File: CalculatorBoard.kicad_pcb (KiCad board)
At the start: 2 copper layers, 81.3 x 83.8 mm, 62 parts, among them J1 Conn_01x07_Male, Q1 Q_NPN_EBC, Q10 Q_NPN_EBC, Q11 Q_NPN_EBC, Q12 Q_NPN_EBC, Q13 Q_NPN_EBC, Q14 Q_NPN_EBC, Q15 Q_NPN_EBC, Q16 Q_NPN_EBC, Q17 Q_NPN_EBC, Q18 Q_NPN_EBC, Q19 Q_NPN_EBC, Q2 Q_NPN_EBC, Q20 Q_NPN_EBC, Q21 Q_NPN_EBC, Q22 Q_NPN_EBC, Q3 Q_NPN_EBC, Q4 Q_NPN_EBC, Q5 Q_NPN_EBC, Q6 Q_NPN_EBC, Q7 Q_NPN_EBC, Q8 Q_NPN_EBC, Q9 Q_NPN_EBC

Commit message: fix pin 5 goof. Reroute some components.
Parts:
- moved R10 17.1 mm to (62.1, 86.4), turned to 270 degrees
- moved R16 16.8 mm to (43.2, 91.4), turned to 90 degrees
- moved Q13 15.9 mm to (51.1, 85.7)
- moved R25 15.1 mm to (28.1, 73.0), turned to 90 degrees
- moved R22 13.4 mm to (54.9, 79.4), turned to 0 degrees
- moved R19 12.7 mm to (54.6, 91.2)
- moved H2 12.2 mm to (21.1, 91.4)
- moved H1 12.1 mm to (95.5, 91.3)
- moved Q5 10.7 mm to (71.1, 65.6)
- moved R13 9.66 mm to (73.2, 75.8)
- moved R14 8.41 mm to (70.0, 86.4), turned to 270 degrees
- moved R24 7.38 mm to (34.7, 86.2)
- moved R30 5.89 mm to (28.5, 91.1)
- moved R35 5.21 mm to (21.6, 34.0), turned to 270 degrees
- moved Q9 4.32 mm to (64.0, 71.1)
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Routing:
- net Net-(Q4-Pad1): track 39.7 -> 21.6 mm
- net Net-(Q10-Pad1): track 85.9 -> 69.2 mm
- net Net-(Q5-Pad1): track 10.8 -> 23.0 mm
- net Net-(Q13-Pad3): track 20.8 -> 29.4 mm
- net Net-(Q5-Pad2): track 38.7 -> 31.5 mm
- net Net-(Q16-Pad1): track 17.8 -> 22.7 mm
- net Net-(Q15-Pad2): track 12.7 -> 8.15 mm
- net Net-(J1-Pad5): track 88.2 -> 92.5 mm
- net Net-(Q16-Pad2): track 12.7 -> 9.25 mm
- net Net-(Q9-Pad2): track 8.15 -> 11.5 mm
- net Net-(Q6-Pad1): track 21.2 -> 18.4 mm
- net Net-(Q10-Pad2): track 8.93 -> 6.14 mm
- net Net-(Q13-Pad2): track 9.61 -> 7.08 mm
- net Net-(Q2-Pad3): track 34.7 -> 32.5 mm
- net Net-(Q4-Pad2): track 9.78 -> 8.38 mm
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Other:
- board size 81.3 x 83.8 mm -> 81.3 x 73.7 mm

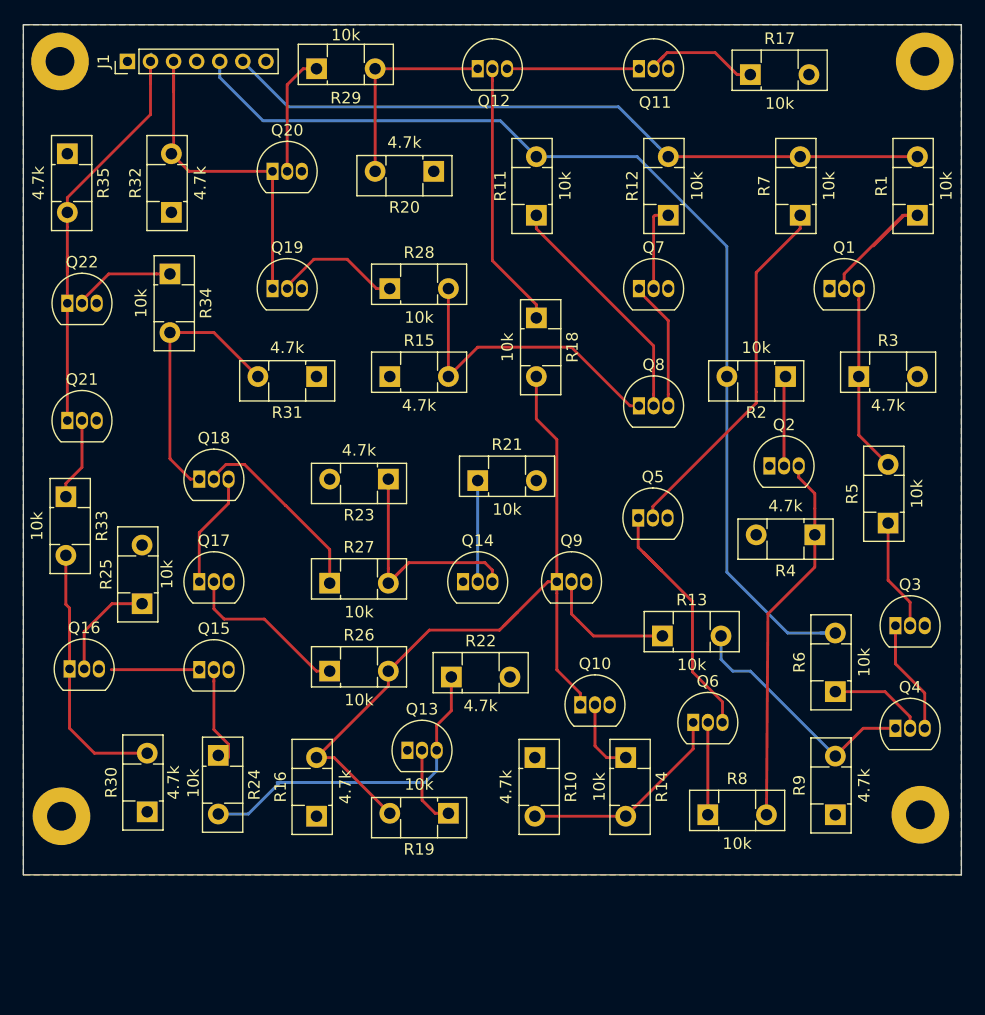
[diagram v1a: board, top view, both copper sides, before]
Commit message: change resistor size and shrink layout
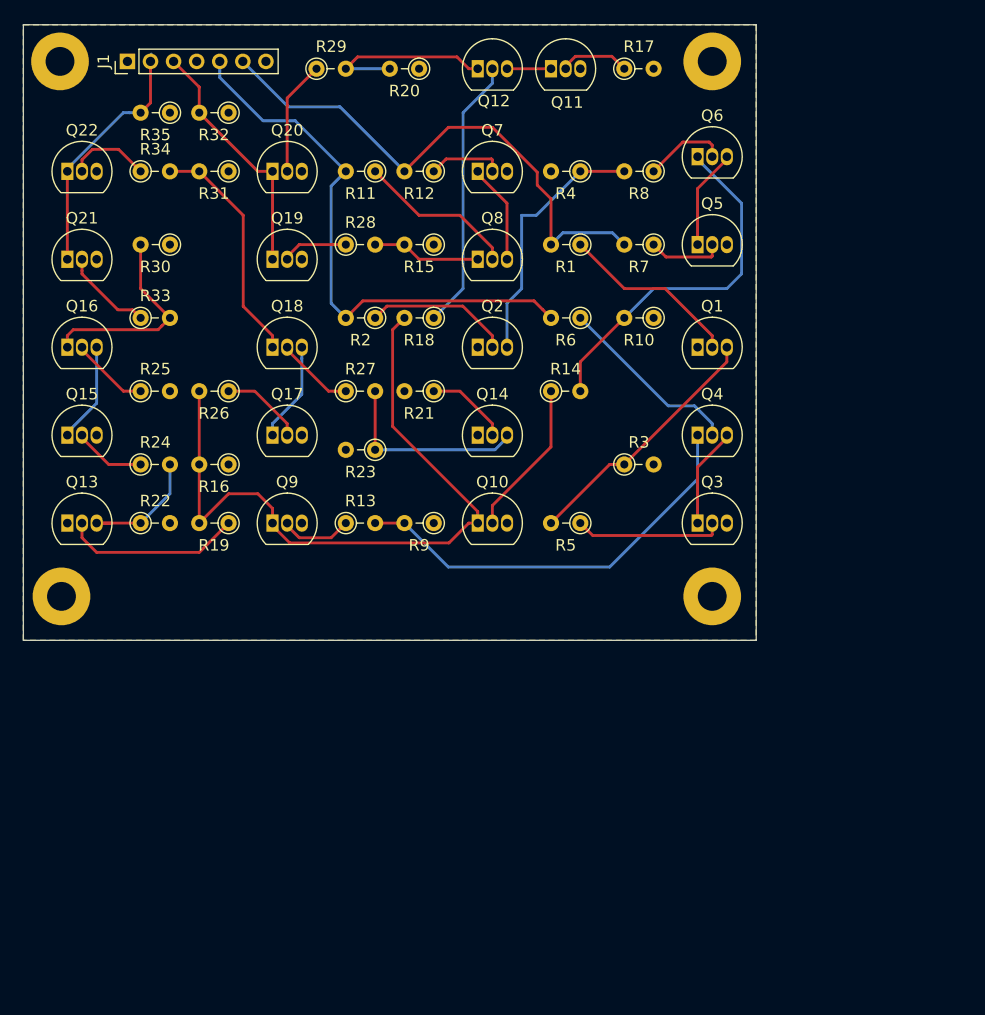
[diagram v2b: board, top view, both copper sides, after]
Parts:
- R1, R10, R11, R12, R13, R14, R15, R16, R17, R18, R19, R2, R20, R21, R22, R23, R24, R25, R26, R27, R28, R29, R3, R30, R31, R32, R33, R34, R35, R4, R5, R6, R7, R8, R9: footprint Package_TO_SOT_THT:TO-126-2_Vertical -> Resistor_THT:R_Axial_DIN0204_L3.6mm_D1.6mm_P2.54mm_Vertical
- moved R8 56.0 mm to (72.4, 35.6), turned to 180 degrees
- moved R30 49.2 mm to (30.5, 41.9), turned to 180 degrees
- moved Q6 49.0 mm to (76.2, 34.3)
- moved R9 43.0 mm to (53.3, 66.0), turned to 180 degrees
- moved R10 39.5 mm to (72.4, 48.3), turned to 180 degrees
- moved R6 39.2 mm to (66.0, 48.3), turned to 180 degrees
- moved R4 37.5 mm to (66.0, 35.6)
- moved R2 35.9 mm to (48.3, 48.3)
- moved Q13 35.4 mm to (21.6, 66.0)
- moved R14 32.4 mm to (63.5, 54.6), turned to 0 degrees
- moved R19 31.5 mm to (35.6, 66.0)
- moved R16 31.4 mm to (35.6, 61.0), turned to 180 degrees
- moved Q4 30.6 mm to (76.2, 58.4)
- moved R22 30.0 mm to (27.9, 66.0)
- moved R1 29.3 mm to (66.0, 41.9), turned to 180 degrees
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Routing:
- net Net-(J1-Pad5): track 92.5 -> 48.4 mm
- net Net-(Q5-Pad2): track 31.5 -> 6.56 mm
- net Net-(Q13-Pad3): track 29.4 -> 11.2 mm
- net Net-(Q8-Pad1): track 27.3 -> 9.42 mm
- net Net-(J1-Pad6): track 61.9 -> 46.6 mm
- net 2: track 37.6 -> 22.7 mm
- net Net-(Q4-Pad1): track 21.6 -> 36.5 mm
- net Net-(Q5-Pad1): track 23.0 -> 8.67 mm
- net Net-(Q6-Pad1): track 18.4 -> 31.4 mm
- net Net-(Q2-Pad3): track 32.5 -> 22.4 mm
- net Net-(Q18-Pad2): track 16.7 -> 6.79 mm
- net 3: track 30.5 -> 21.4 mm
- net Net-(Q13-Pad2): track 7.08 -> 15.8 mm
- net Net-(Q10-Pad1): track 69.2 -> 61.2 mm
- net Net-(Q4-Pad2): track 8.38 -> 16.2 mm
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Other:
- board size 81.3 x 73.7 mm -> 63.5 x 53.3 mm

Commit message: minor tweaks
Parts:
- moved R25 6.35 mm to (27.9, 48.3)
- moved R33 6.35 mm to (27.9, 41.9)
- moved R30 5.08 mm to (35.6, 41.9)
- moved R5 5.08 mm to (71.1, 66.0)
- moved R23 1.27 mm to (48.3, 61.0)
- moved R3 1.27 mm to (68.6, 61.0)
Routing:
- net Net-(Q3-Pad2): track 12.9 -> 9.20 mm
- net Net-(Q14-Pad3): track 17.2 -> 19.6 mm
- net Net-(Q4-Pad1): track 36.5 -> 38.7 mm
- net Net-(Q21-Pad2): track 7.93 -> 5.74 mm
- net Net-(Q16-Pad1): track 17.9 -> 16.6 mm
- net Net-(Q1-Pad3): track 22.3 -> 21.1 mm

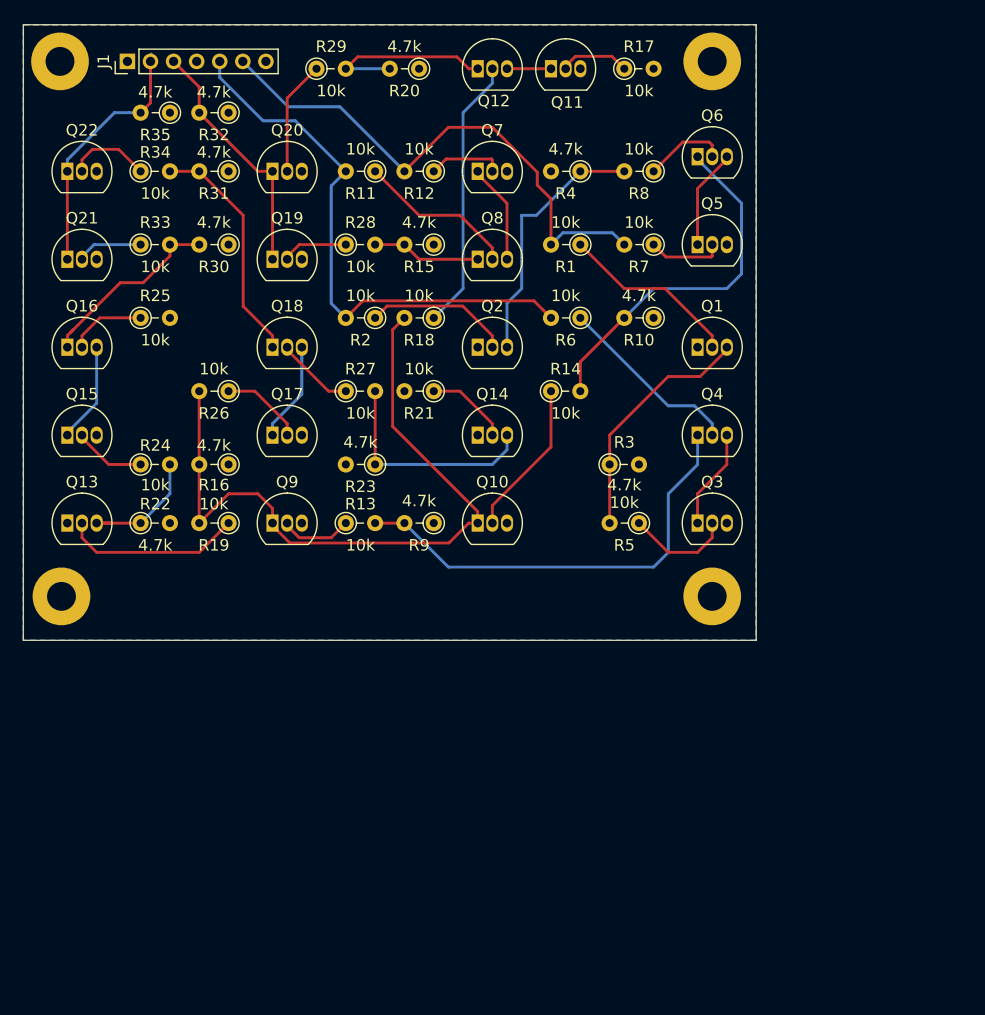
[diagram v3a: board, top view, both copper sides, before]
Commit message: clean up some traces
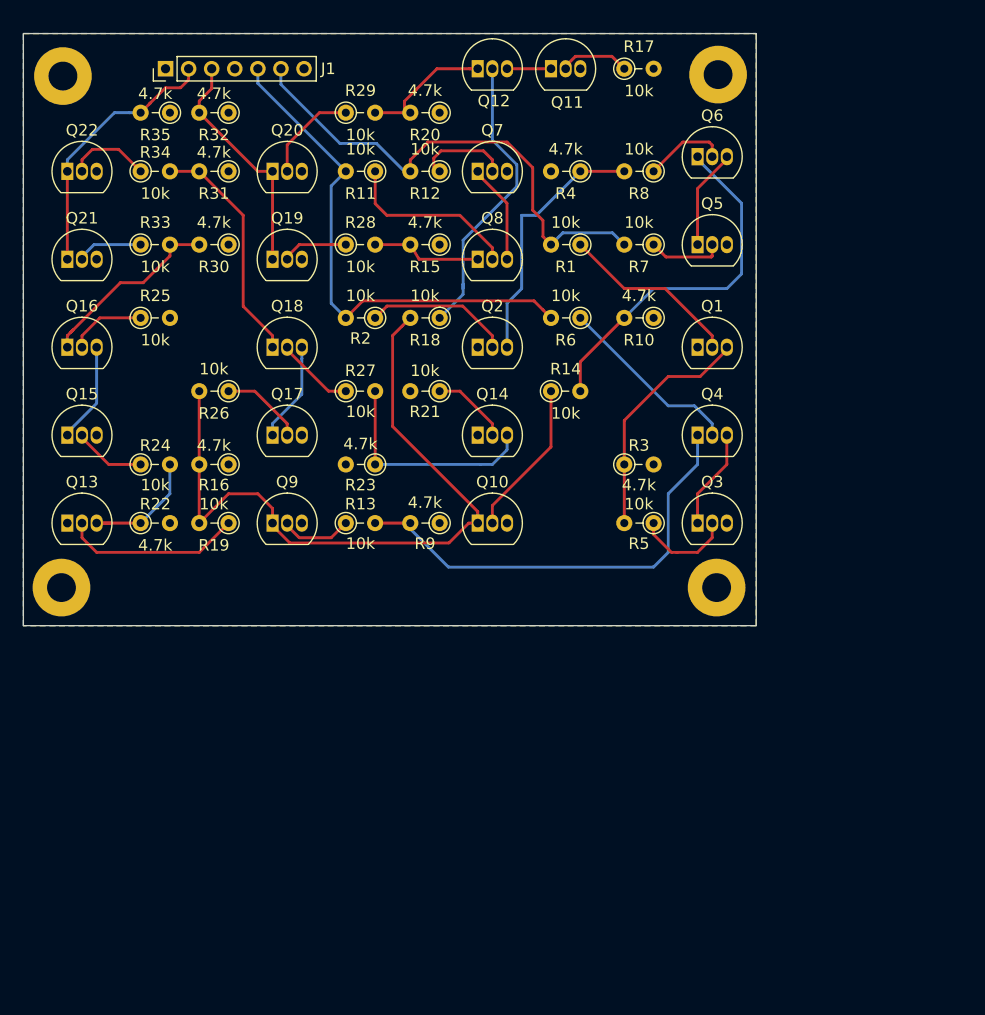
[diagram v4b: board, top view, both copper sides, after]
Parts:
- moved R29 4.58 mm to (45.7, 30.5)
- moved R20 4.20 mm to (53.8, 30.5)
- moved J1 3.36 mm to (30.1, 26.7)
- moved H4 1.30 mm to (21.2, 27.3)
- moved R3 1.27 mm to (69.8, 61.0)
- moved R5 1.27 mm to (72.4, 66.0)
- moved H3 1.25 mm to (78.0, 27.2)
- moved H1 0.85 mm to (77.9, 71.6)
- moved H2 0.76 mm to (21.1, 71.6)
- moved R12 0.51 mm to (53.8, 35.6)
- moved R15 0.51 mm to (53.8, 41.9)
- moved R18 0.51 mm to (53.8, 48.3)
- moved R21 0.51 mm to (53.8, 54.6)
- moved R9 0.51 mm to (53.8, 66.0)
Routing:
- net Net-(Q12-Pad1): track 16.1 -> 12.2 mm
- net Net-(J1-Pad6): track 46.6 -> 42.9 mm
- net Net-(J1-Pad5): track 48.4 -> 44.8 mm
- net Net-(Q12-Pad2): track 23.7 -> 25.6 mm
- net Net-(Q8-Pad2): track 13.9 -> 15.5 mm
- net Net-(Q20-Pad2): track 9.94 -> 8.52 mm
- net Net-(Q7-Pad2): track 6.56 -> 7.91 mm
- net 3: track 21.4 -> 20.3 mm
- net Net-(Q3-Pad2): track 9.20 -> 8.51 mm
- net Net-(Q1-Pad3): track 21.1 -> 20.5 mm
- net Net-(Q4-Pad1): track 38.7 -> 39.2 mm
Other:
- board size 63.5 x 53.3 mm -> 63.5 x 51.3 mm
